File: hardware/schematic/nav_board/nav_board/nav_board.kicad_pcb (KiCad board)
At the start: 2 copper layers, 98.4 x 36.2 mm, 6 parts, among them J1 Display, J2 Flow Meter, J3 Depth Sensor, J4 GPS

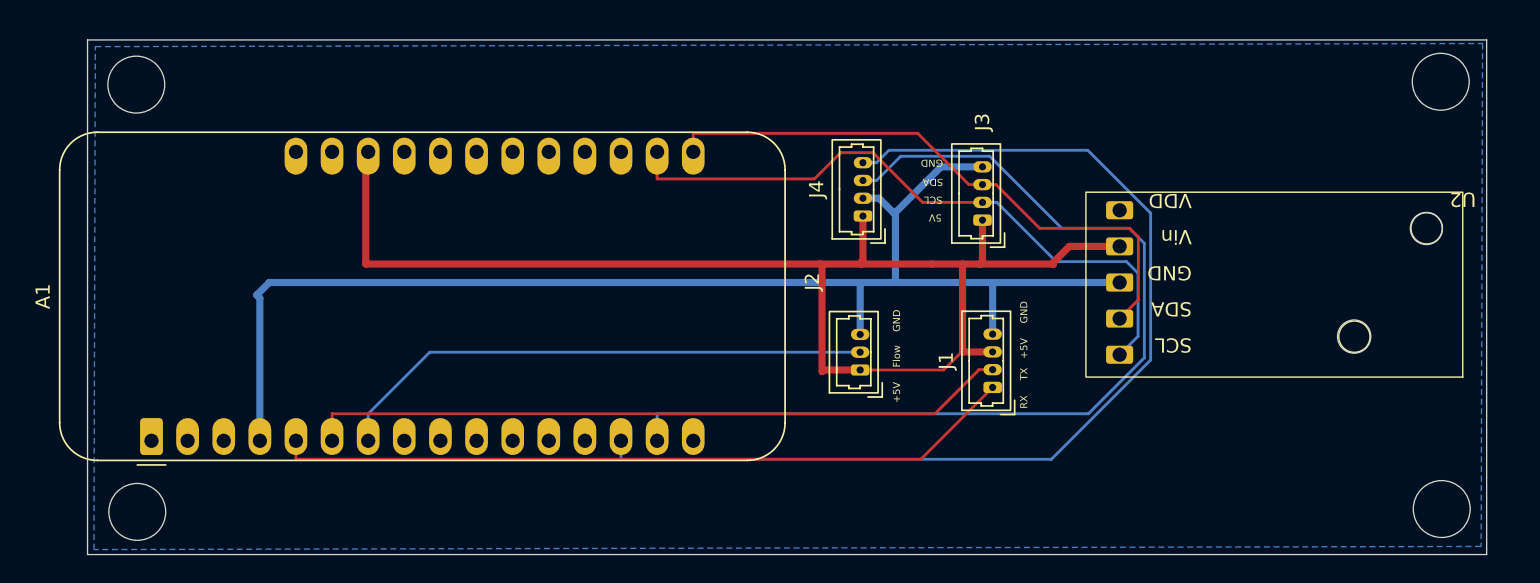
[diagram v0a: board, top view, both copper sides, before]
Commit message: Consolidate display_board/nav_board KiCad files to latest local work
This machine has the most recent hardware design work. Promote the
Rev B design to canonical display_board.kicad_pro/.kicad_sch/.kicad_pcb,
move its matching gerbers/drill files into manufacturing/, track the
gopro-housing variant as a maintained alternate board, and drop the
superseded Rev A files, stale fabrication/ output, and backup zips
(archived locally under a gitignored _archive/ folder rather than
deleted outright). Also brings nav_board's schematic/PCB/manufacturing
files up to date.

Co-Authored-By: Claude Sonnet 5 <noreply@anthropic.com>
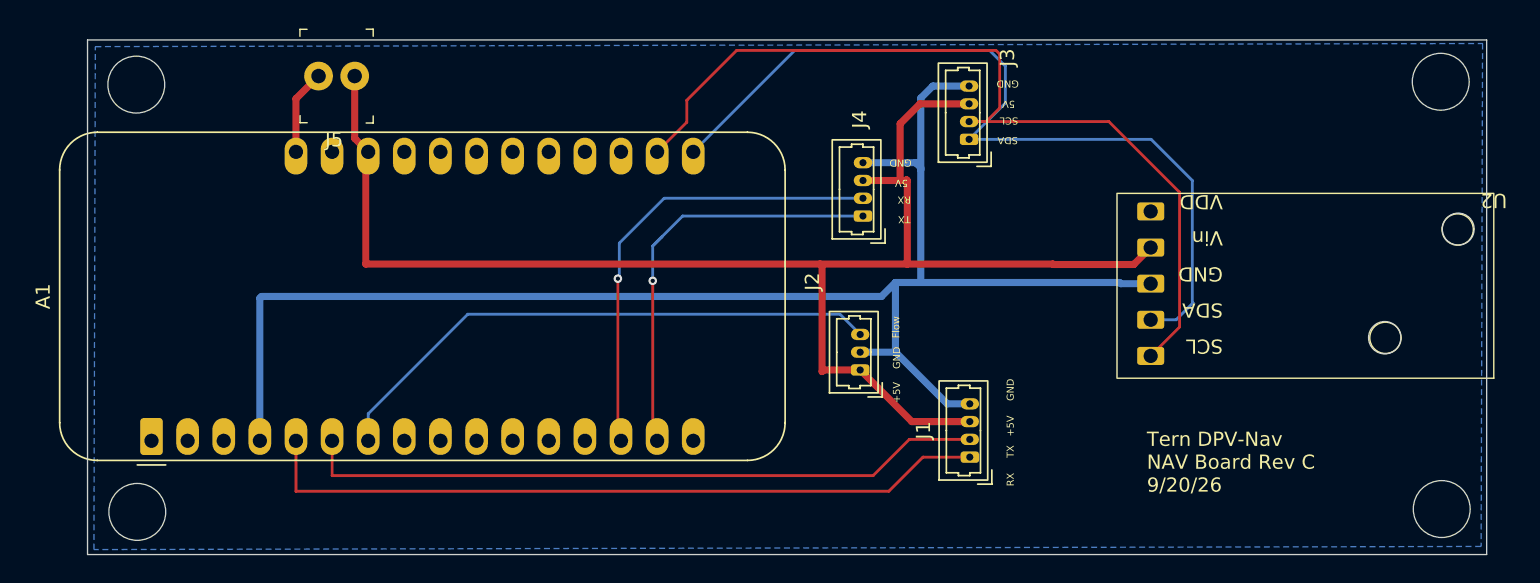
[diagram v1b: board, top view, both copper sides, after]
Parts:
- added J5: USB to BAT, digikey-footprints:PinHeader_1x2_P2.54mm_Drill1.02mm, F.Cu at (44.3, 37.4)
- J2: value Flow Meter -> Flow
- J3: value Depth Sensor -> Depth
- moved J3 5.76 mm to (87.5, 41.8)
- moved J1 5.16 mm to (87.5, 64.2)
- moved U2 2.18 mm to (124.4, 45.6)
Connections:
- A1 pad 28: unconnected-(A1-VBAT-Pad28) -> Net-(A1-VBAT)
- J2 pad 2: Net-(A1-I34/A2) -> GND
- J2 pad 3: GND -> Net-(A1-I34/A2)
- J3 pad 1: +5V -> Net-(A1-SDA/IO23)
- J3 pad 3: Net-(A1-SDA/IO23) -> +5V
- J4 pad 1: +5V -> Net-(A1-TX/IO17)
- J4 pad 2: GND -> Net-(A1-RX/IO16)
- J4 pad 3: Net-(A1-TX/IO17) -> +5V
- J4 pad 4: Net-(A1-RX/IO16) -> GND
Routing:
- net Net-(A1-RX/IO16): track 74.2 -> 32.5 mm, vias 0 -> 1
- net Net-(A1-TX/IO17): track 68.9 -> 30.3 mm, vias 0 -> 1
- net Net-(A1-SDA/IO23): track 41.9 -> 60.6 mm
- net Net-(A1-SCL/IO22): track 46.3 -> 63.6 mm
- net GND: track 93.6 -> 108.1 mm
- net +5V: track 94.5 -> 107.4 mm
- net Net-(A1-VBAT): track 0.00 -> 5.99 mm
- net Net-(A1-I34/A2): track 38.3 -> 40.0 mm
- net Net-(A1-DAC1/A1): track 49.6 -> 48.4 mm
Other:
- outline, holes or cut-outs redrawn
- board text added: "Tern DPV-Nav NAV Board Rev C 9/20/26"
